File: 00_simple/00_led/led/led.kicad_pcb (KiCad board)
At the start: 2 copper layers, 0 parts

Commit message: draw edge
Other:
- board outline added: 25.4 x 25.4 mm
- net class Default: trace_width 0.25 -> 0.254
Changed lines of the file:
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@@
   (general
     (thickness 1.6)
-    (drawings 0)
+    (drawings 4)
     (tracks 0)
     (zones 0)
@@
   )
   (setup
-    (last_trace_width 0.25)
+    (last_trace_width 0.254)
     (trace_clearance 0.2)
     (zone_clearance 0.508)
@@
   (net_class Default "This is the default net class."
     (clearance 0.2)
-    (trace_width 0.25)
+    (trace_width 0.254)
     (via_dia 0.8)
     (via_drill 0.4)
@@
     (uvia_drill 0.1)
   )
+  (gr_line (start 127 114.3) (end 127 88.9) (layer Edge.Cuts) (width 0.15))
+  (gr_line (start 152.4 114.3) (end 127 114.3) (layer Edge.Cuts) (width 0.15))
+  (gr_line (start 152.4 88.9) (end 152.4 114.3) (layer Edge.Cuts) (width 0.15))
+  (gr_line (start 127 88.9) (end 152.4 88.9) (layer Edge.Cuts) (width 0.15))
 )

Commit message: set parts
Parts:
- added D1: OSR5JA3Z74A, LED_THT:LED_D3.0mm, F.Cu at (149.9, 94.0)
- added R1: 640, Resistor_THT:R_Axial_DIN0207_L6.3mm_D2.5mm_P7.62mm_Horizontal, F.Cu at (129.5, 94.0)
- added SW1: SW_SPST, mylib:TVGP01-G73BB, F.Cu at (135.9, 106.7)
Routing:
- net Net-(R1-Pad1): track 0.00 -> 10.2 mm
- net Net-(D1-Pad2): track 0.00 -> 10.2 mm
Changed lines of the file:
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@@
     (thickness 1.6)
     (drawings 4)
-    (tracks 0)
+    (tracks 2)
     (zones 0)
-    (modules 0)
-    (nets 1)
+    (modules 3)
+    (nets 5)
   )
   (page A4)
@@
     (pad_to_mask_clearance 0.2)
     (aux_axis_origin 0 0)
+    (grid_origin 127 88.9)
     (visible_elements FFFFFF7F)
     (pcbplotparams
@@
   )
   (net 0 "")
+  (net 1 GND)
+  (net 2 "Net-(D1-Pad2)")
+  (net 3 "Net-(R1-Pad1)")
+  (net 4 "Net-(SW1-Pad2)")
   (net_class Default "This is the default net class."
     (clearance 0.2)
@@
     (uvia_dia 0.3)
     (uvia_drill 0.1)
+    (add_net GND)
+    (add_net "Net-(D1-Pad2)")
+    (add_net "Net-(R1-Pad1)")
+    (add_net "Net-(SW1-Pad2)")
+  )
+  (module LED_THT:LED_D3.0mm (layer F.Cu)
+    (at 149.86 93.98 180)
+    (descr "LED, diameter 3.0mm, 2 pins")
+    (tags "LED diameter 3.0mm 2 pins")
+    (fp_text reference D1 (at 1.27 -2.96 180) (layer F.SilkS)
+      (effects (font (size 1 1) (thickness 0.15)))
+    )
+    (fp_text value OSR5JA3Z74A (at 1.27 2.96 180) (layer F.Fab)
+      (effects (font (size 1 1) (thickness 0.15)))
+    )
+    (fp_arc (start 1.27 0) (end -0.23 -1.16619) (angle 284.3) (layer F.Fab) (width 0.1))
+    (fp_arc (start 1.27 0) (end -0.29 -1.235516) (angle 108.8) (layer F.SilkS) (width 0.12))
+    (fp_arc (start 1.27 0) (end -0.29 1.235516) (angle -108.8) (layer F.SilkS) (width 0.12))
+    (fp_arc (start 1.27 0) (end 0.229039 -1.08) (angle 87.9) (layer F.SilkS) (width 0.12))
+    (fp_arc (start 1.27 0) (end 0.229039 1.08) (angle -87.9) (layer F.SilkS) (width 0.12))
+    (fp_circle (center 1.27 0) (end 2.77 0) (layer F.Fab) (width 0.1))
+    (fp_line (start -0.23 -1.16619) (end -0.23 1.16619) (layer F.Fab) (width 0.1))
+    (fp_line (start -0.29 -1.236) (end -0.29 -1.08) (layer F.SilkS) (width 0.12))
+    (fp_line (start -0.29 1.08) (end -0.29 1.236) (layer F.SilkS) (width 0.12))
+    (fp_line (start -1.15 -2.25) (end -1.15 2.25) (layer F.CrtYd) (width 0.05))
+    (fp_line (start -1.15 2.25) (end 3.7 2.25) (layer F.CrtYd) (width 0.05))
+    (fp_line (start 3.7 2.25) (end 3.7 -2.25) (layer F.CrtYd) (width 0.05))
+    (fp_line (start 3.7 -2.25) (end -1.15 -2.25) (layer F.CrtYd) (width 0.05))
+    (pad 1 thru_hole rect (at 0 0 180) (size 1.8 1.8) (drill 0.9) (layers *.Cu *.Mask)
+      (net 1 GND))
+    (pad 2 thru_hole circle (at 2.54 0 180) (size 1.8 1.8) (drill 0.9) (layers *.Cu *.Mask)
+      (net 2 "Net-(D1-Pad2)"))
+    (model ${KISYS3DMOD}/LED_THT.3dshapes/LED_D3.0mm.wrl
+      (at (xyz 0 0 0))
+      (scale (xyz 1 1 1))
+      (rotate (xyz 0 0 0))
+    )
+  )
+  (module Resistor_THT:R_Axial_DIN0207_L6.3mm_D2.5mm_P7.62mm_Horizontal (layer F.Cu)
+    (at 129.54 93.98)
+    (descr "Resistor, Axial_DIN0207 series, Axial, Horizontal, pin pitch=7.62mm, 0.25W = 1/4W, length*diameter=6.3*2.5mm^2, http://cdn-reichelt.de/documents/datenblatt/B400/1_4W%23YAG.pdf")
+    (tags "Resistor Axial_DIN0207 series Axial Horizontal pin pitch 7.62mm 0.25W = 1/4W length 6.3mm diameter 2.5mm")
+    (fp_text reference R1 (at 3.81 -2.37) (layer F.SilkS)
+      (effects (font (size 1 1) (thickness 0.15)))
+    )
+    (fp_text value 640 (at 3.81 2.37) (layer F.Fab)
+      (effects (font (size 1 1) (thickness 0.15)))
+    )
+    (fp_line (start 0.66 -1.25) (end 0.66 1.25) (layer F.Fab) (width 0.1))
+    (fp_line (start 0.66 1.25) (end 6.96 1.25) (layer F.Fab) (width 0.1))
+    (fp_line (start 6.96 1.25) (end 6.96 -1.25) (layer F.Fab) (width 0.1))
+    (fp_line (start 6.96 -1.25) (end 0.66 -1.25) (layer F.Fab) (width 0.1))
+    (fp_line (start 0 0) (end 0.66 0) (layer F.Fab) (width 0.1))
+    (fp_line (start 7.62 0) (end 6.96 0) (layer F.Fab) (width 0.1))
+    (fp_line (start 0.54 -1.04) (end 0.54 -1.37) (layer F.SilkS) (width 0.12))
+    (fp_line (start 0.54 -1.37) (end 7.08 -1.37) (layer F.SilkS) (width 0.12))
+    (fp_line (start 7.08 -1.37) (end 7.08 -1.04) (layer F.SilkS) (width 0.12))
+    (fp_line (start 0.54 1.04) (end 0.54 1.37) (layer F.SilkS) (width 0.12))
+    (fp_line (start 0.54 1.37) (end 7.08 1.37) (layer F.SilkS) (width 0.12))
+    (fp_line (start 7.08 1.37) (end 7.08 1.04) (layer F.SilkS) (width 0.12))
+    (fp_line (start -1.05 -1.5) (end -1.05 1.5) (layer F.CrtYd) (width 0.05))
+    (fp_line (start -1.05 1.5) (end 8.67 1.5) (layer F.CrtYd) (width 0.05))
+    (fp_line (start 8.67 1.5) (end 8.67 -1.5) (layer F.CrtYd) (width 0.05))
+    (fp_line (start 8.67 -1.5) (end -1.05 -1.5) (layer F.CrtYd) (width 0.05))
+    (fp_text user %R (at 3.81 0) (layer F.Fab)
+      (effects (font (size 1 1) (thickness 0.15)))
+    )
+    (pad 1 thru_hole circle (at 0 0) (size 1.6 1.6) (drill 0.8) (layers *.Cu *.Mask)
+      (net 3 "Net-(R1-Pad1)"))
+    (pad 2 thru_hole oval (at 7.62 0) (size 1.6 1.6) (drill 0.8) (layers *.Cu *.Mask)
+      (net 2 "Net-(D1-Pad2)"))
+    (model ${KISYS3DMOD}/Resistor_THT.3dshapes/R_Axial_DIN0207_L6.3mm_D2.5mm_P7.62mm_Horizontal.wrl
+      (at (xyz 0 0 0))
+      (scale (xyz 1 1 1))
+      (rotate (xyz 0 0 0))
+    )
+  )
+  (module mylib:TVGP01-G73BB (layer F.Cu)
+    (at 135.89 106.68)
+    (fp_text reference SW1 (at 0 -7.62) (layer F.SilkS)
+      (effects (font (size 1 1) (thickness 0.15)))
+    )
+    (fp_text value SW_SPST (at 0 -10.16) (layer F.Fab)
+      (effects (font (size 1 1) (thickness 0.15)))
+    )
+    (fp_line (start -6 -6) (end 6 -6) (layer F.SilkS) (width 0.15))
+    (fp_line (start 6 -6) (end 6 5) (layer F.SilkS) (width 0.15))
+    (fp_line (start 6 5) (end -6 5) (layer F.SilkS) (width 0.15))
+    (fp_line (start -6 5) (end -6 -6) (layer F.SilkS) (width 0.15))
+    (pad 1 thru_hole circle (at -6.35 -2.54) (size 1.6 1.6) (drill 0.8) (layers *.Cu *.Mask)
+      (net 3 "Net-(R1-Pad1)"))
+    (pad 2 thru_hole circle (at 6.35 -2.54) (size 1.6 1.6) (drill 0.8) (layers *.Cu *.Mask)
+      (net 4 "Net-(SW1-Pad2)"))
+    (pad 3 thru_hole circle (at -6.35 2.54) (size 1.6 1.6) (drill 0.8) (layers *.Cu *.Mask))
+    (pad 4 thru_hole circle (at 6.35 2.54) (size 1.6 1.6) (drill 0.8) (layers *.Cu *.Mask))
   )
   (gr_line (start 127 114.3) (end 127 88.9) (layer Edge.Cuts) (width 0.15))
@@
   (gr_line (start 152.4 88.9) (end 152.4 114.3) (layer Edge.Cuts) (width 0.15))
   (gr_line (start 127 88.9) (end 152.4 88.9) (layer Edge.Cuts) (width 0.15))
+  (segment (start 137.16 93.98) (end 147.32 93.98) (width 0.254) (layer F.Cu) (net 2))
+  (segment (start 129.54 93.98) (end 129.54 104.14) (width 0.254) (layer F.Cu) (net 3))
 )

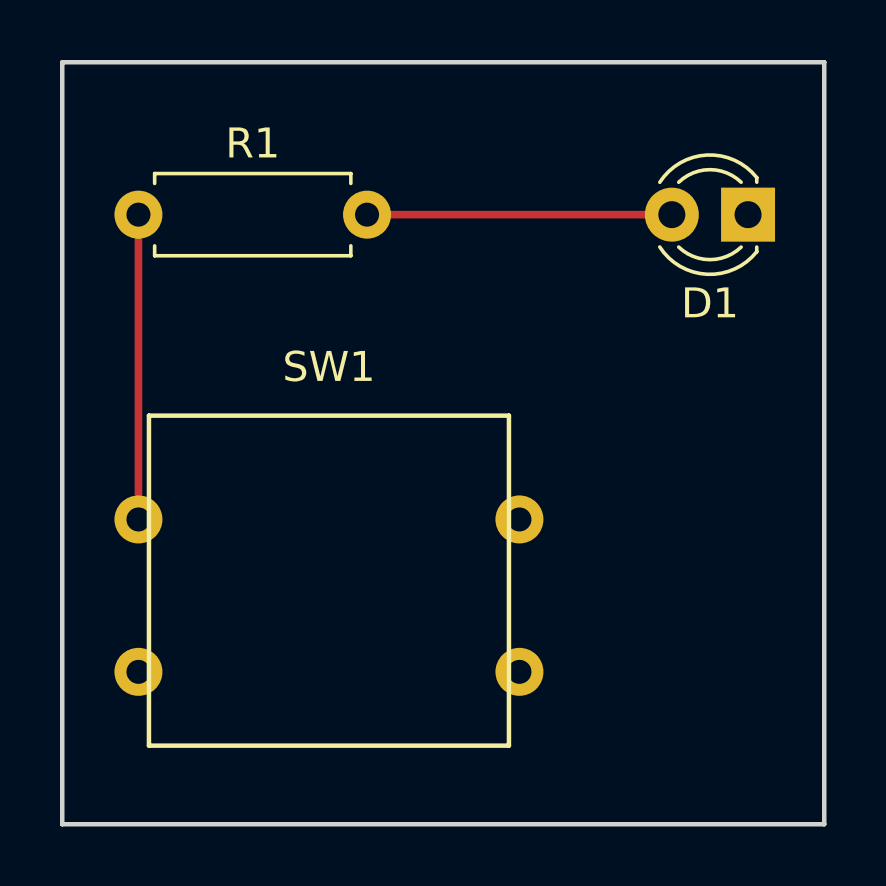
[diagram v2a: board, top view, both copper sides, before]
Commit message: add pinheader
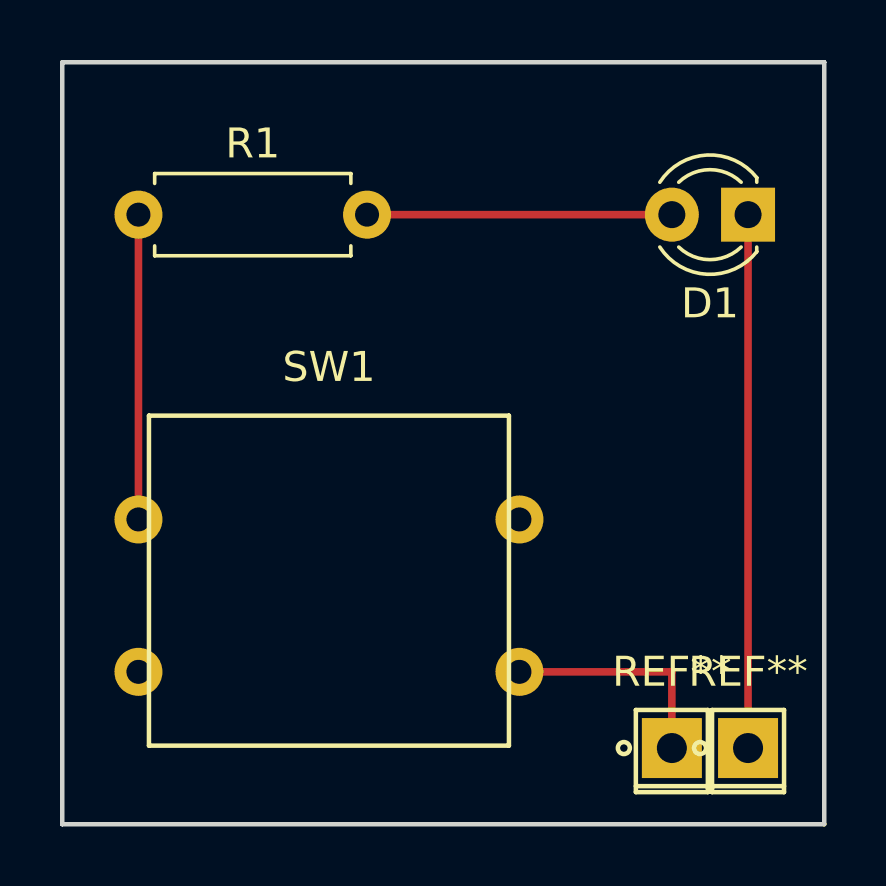
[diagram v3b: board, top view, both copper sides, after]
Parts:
- added REF**: PINHEADER_1x1, mylib:PINHEADER_1x1, F.Cu at (149.9, 111.8)
- added REF**: PINHEADER_1x1, mylib:PINHEADER_1x1, F.Cu at (147.3, 111.8)
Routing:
- net GND: track 0.00 -> 16.5 mm
- net (no net): track 0.00 -> 7.62 mm
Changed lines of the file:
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@@
     (thickness 1.6)
     (drawings 4)
-    (tracks 2)
+    (tracks 5)
     (zones 0)
-    (modules 3)
+    (modules 5)
     (nets 5)
   )
@@
     (pad 4 thru_hole circle (at 6.35 2.54) (size 1.6 1.6) (drill 0.8) (layers *.Cu *.Mask))
   )
+  (module mylib:PINHEADER_1x1 (layer F.Cu)
+    (at 149.86 111.76)
+    (fp_text reference REF** (at 0 -2.54) (layer F.SilkS)
+      (effects (font (size 1 1) (thickness 0.15)))
+    )
+    (fp_text value PINHEADER_1x1 (at 0 -4.54) (layer F.Fab) hide
+      (effects (font (size 1 1) (thickness 0.15)))
+    )
+    (fp_circle (center -1.6 0) (end -1.6 0.2) (layer F.SilkS) (width 0.15))
+    (fp_line (start -1.2 1.27) (end 1.2 1.27) (layer F.SilkS) (width 0.15))
+    (fp_line (start -1.2 1.47) (end -1.2 -1.27) (layer F.SilkS) (width 0.15))
+    (fp_line (start 1.2 1.47) (end -1.2 1.47) (layer F.SilkS) (width 0.15))
+    (fp_line (start 1.2 -1.27) (end 1.2 1.47) (layer F.SilkS) (width 0.15))
+    (fp_line (start -1.2 -1.27) (end 1.2 -1.27) (layer F.SilkS) (width 0.15))
+    (pad 1 thru_hole rect (at 0 0) (size 2 2) (drill 1) (layers *.Cu *.Mask F.SilkS))
+  )
+  (module mylib:PINHEADER_1x1 (layer F.Cu)
+    (at 147.32 111.76)
+    (fp_text reference REF** (at 0 -2.54) (layer F.SilkS)
+      (effects (font (size 1 1) (thickness 0.15)))
+    )
+    (fp_text value PINHEADER_1x1 (at 0 -4.54) (layer F.Fab) hide
+      (effects (font (size 1 1) (thickness 0.15)))
+    )
+    (fp_circle (center -1.6 0) (end -1.6 0.2) (layer F.SilkS) (width 0.15))
+    (fp_line (start -1.2 1.27) (end 1.2 1.27) (layer F.SilkS) (width 0.15))
+    (fp_line (start -1.2 1.47) (end -1.2 -1.27) (layer F.SilkS) (width 0.15))
+    (fp_line (start 1.2 1.47) (end -1.2 1.47) (layer F.SilkS) (width 0.15))
+    (fp_line (start 1.2 -1.27) (end 1.2 1.47) (layer F.SilkS) (width 0.15))
+    (fp_line (start -1.2 -1.27) (end 1.2 -1.27) (layer F.SilkS) (width 0.15))
+    (pad 1 thru_hole rect (at 0 0) (size 2 2) (drill 1) (layers *.Cu *.Mask F.SilkS))
+  )
   (gr_line (start 127 114.3) (end 127 88.9) (layer Edge.Cuts) (width 0.15))
   (gr_line (start 152.4 114.3) (end 127 114.3) (layer Edge.Cuts) (width 0.15))
   (gr_line (start 152.4 88.9) (end 152.4 114.3) (layer Edge.Cuts) (width 0.15))
   (gr_line (start 127 88.9) (end 152.4 88.9) (layer Edge.Cuts) (width 0.15))
+  (segment (start 147.32 111.76) (end 147.32 109.22) (width 0.254) (layer F.Cu) (net 0))
+  (segment (start 147.32 109.22) (end 142.24 109.22) (width 0.254) (layer F.Cu) (net 0))
+  (segment (start 149.86 93.98) (end 149.86 110.432999) (width 0.254) (layer F.Cu) (net 1))
   (segment (start 137.16 93.98) (end 147.32 93.98) (width 0.254) (layer F.Cu) (net 2))
   (segment (start 129.54 93.98) (end 129.54 104.14) (width 0.254) (layer F.Cu) (net 3))
